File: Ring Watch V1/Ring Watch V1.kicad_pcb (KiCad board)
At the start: 2 copper layers, 28 x 20.8 mm, 12 parts, among them J1 Programming Header, J2 CR2023 Socket, U1 ATtiny85-20SU, U2 PCF8523T, Y1 32.768

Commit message: almost done placing components
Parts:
- C2: moved to F.Cu
- J1: footprint Connector_PinHeader_2.54mm:PinHeader_2x03_P2.54mm_Vertical -> Connector_PinHeader_1.00mm:PinHeader_2x03_P1.00mm_Vertical
- moved C1 20.2 mm to (108.7, 112.3), turned to 90 degrees
- moved R1 16.1 mm to (100.1, 107.4), turned to 270 degrees
- moved C2 13.8 mm to (97.4, 113.5)
- moved R3 13.0 mm to (108.5, 105.7), turned to 270 degrees
- moved J1 12.9 mm to (112.0, 109.0)
- moved U1 1.53 mm to (104.3, 109.1), turned to 270 degrees
- moved U2 0.51 mm to (95.9, 108.5)
- moved Y1 0.51 mm to (90.8, 108.5)
- moved R2 0.41 mm to (104.4, 102.6)
- moved D1 0.35 mm to (98.3, 101.5)
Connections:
- J1 pad 5: B3 -> B5
- U2 pad 8: +BATT -> Net-(C1-Pad1)
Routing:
- net B2: track 0.00 -> 11.1 mm, vias 0 -> 1
- net B0: track 0.00 -> 10.0 mm
- net B4: track 0.00 -> 7.23 mm
- net B1: track 0.00 -> 7.18 mm
- net B3: track 0.00 -> 3.07 mm

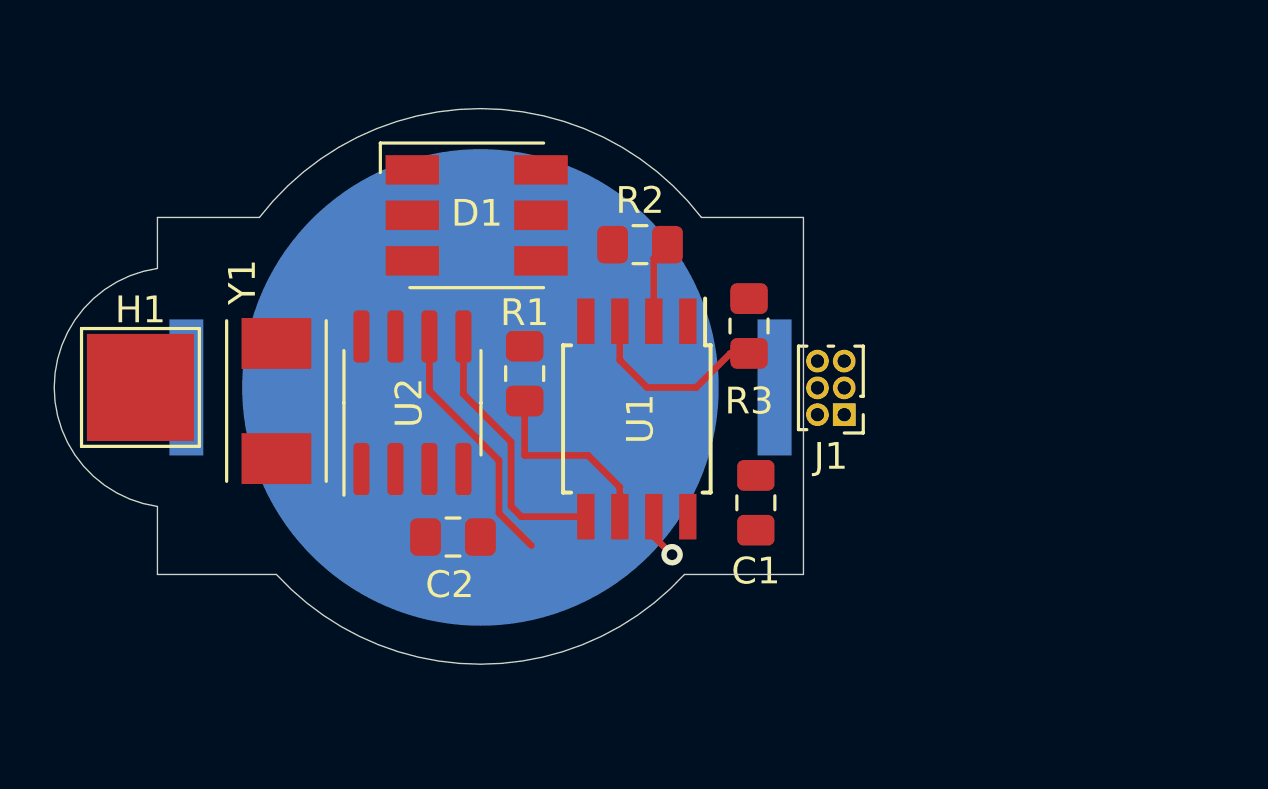
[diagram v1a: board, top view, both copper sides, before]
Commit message: modified component placement
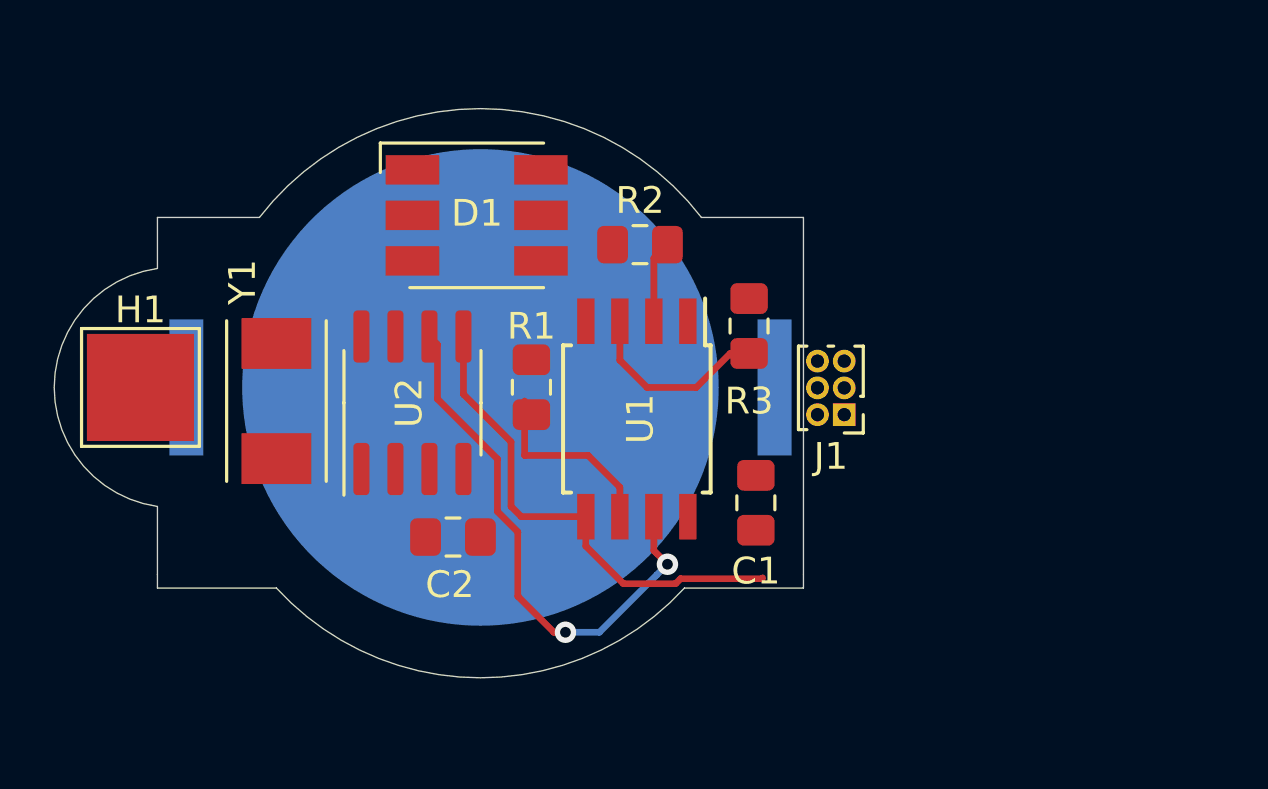
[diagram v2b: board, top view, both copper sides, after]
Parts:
- moved R1 0.57 mm to (100.3, 107.9)
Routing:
- net B2: track 11.1 -> 20.3 mm, vias 1 -> 2
- net B0: track 10.0 -> 18.4 mm
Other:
- board size 28 x 20.8 mm -> 28 x 21.3 mm
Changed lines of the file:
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@@
   (general
     (thickness 1.6)
-    (drawings 10)
-    (tracks 23)
+    (drawings 12)
+    (tracks 38)
     (zones 0)
     (modules 12)
@@
   )
   (module Resistor_SMD:R_0805_2012Metric_Pad1.15x1.40mm_HandSolder (layer F.Cu)
-    (at 100.076 107.433 270)
+    (at 100.33 107.941 270)
     (descr "Resistor SMD 0805 (2012 Metric), square (rectangular) end terminal, IPC_7351 nominal with elongated pad for handsoldering. (Body size source: https://docs.google.com/spreadsheets/d/1BsfQQcO9C6DZCsRaXUlFlo91Tg2WpOkGARC1WS5S8t0/edit?usp=sharing), generated with kicad-footprint-generator")
     (tags "resistor handsolder")
@@
     )
   )
+  (gr_line (start 86.36 114.935) (end 86.36 115.443) (layer Edge.Cuts) (width 0.05))
+  (gr_line (start 110.49 114.935) (end 110.49 115.443) (layer Edge.Cuts) (width 0.05))
+  (gr_arc (start 98.425 108.458) (end 90.805001 115.442999) (angle -94.97910584) (layer Edge.Cuts) (width 0.05))
+  (gr_line (start 110.49 115.443) (end 106.044999 115.442999) (layer Edge.Cuts) (width 0.05))
   (gr_line (start 86.359999 112.394999) (end 86.36 114.935) (layer Edge.Cuts) (width 0.05))
   (gr_line (start 86.36 101.6) (end 86.360001 103.505001) (layer Edge.Cuts) (width 0.05))
   (gr_arc (start 86.995 107.95) (end 86.360001 103.505001) (angle -163.7397953) (layer Edge.Cuts) (width 0.05))
-  (gr_line (start 90.805001 114.934999) (end 86.36 114.935) (layer Edge.Cuts) (width 0.05))
-  (gr_line (start 110.49 114.935) (end 106.044999 114.934999) (layer Edge.Cuts) (width 0.05))
+  (gr_line (start 90.805001 115.442999) (end 86.36 115.443) (layer Edge.Cuts) (width 0.05))
   (gr_line (start 106.679999 101.600001) (end 110.49 101.6) (layer Edge.Cuts) (width 0.05))
   (gr_line (start 86.36 101.6) (end 90.17 101.6) (layer Edge.Cuts) (width 0.05))
-  (gr_arc (start 98.425 107.95) (end 90.805001 114.934999) (angle -94.97910584) (layer Edge.Cuts) (width 0.05))
   (gr_arc (start 98.425 107.95) (end 106.679999 101.600001) (angle -104.8628159) (layer Edge.Cuts) (width 0.05))
   (gr_line (start 110.49 101.6) (end 110.49 114.935) (layer Edge.Cuts) (width 0.05))
@@
   (segment (start 99.95041 112.776) (end 102.362 112.776) (width 0.25) (layer F.Cu) (net 6))
   (segment (start 99.568 112.39359) (end 99.95041 112.776) (width 0.25) (layer F.Cu) (net 6))
+  (segment (start 105.900022 115.09299) (end 108.93501 115.09299) (width 0.25) (layer F.Cu) (net 6))
+  (segment (start 105.71399 115.279022) (end 105.900022 115.09299) (width 0.25) (layer F.Cu) (net 6))
+  (segment (start 103.765021 115.279021) (end 105.71399 115.279022) (width 0.25) (layer F.Cu) (net 6))
+  (segment (start 102.362 112.776) (end 102.362 113.876) (width 0.25) (layer F.Cu) (net 6))
+  (segment (start 102.362 113.876) (end 103.765021 115.279021) (width 0.25) (layer F.Cu) (net 6))
+  (segment (start 108.93501 115.09299) (end 108.966 115.062) (width 0.25) (layer F.Cu) (net 6))
   (segment (start 103.632 111.676) (end 103.632 112.776) (width 0.25) (layer F.Cu) (net 7))
-  (segment (start 102.446 110.49) (end 103.632 111.676) (width 0.25) (layer F.Cu) (net 7))
   (segment (start 100.076 110.49) (end 102.446 110.49) (width 0.25) (layer F.Cu) (net 7))
   (segment (start 100.076 108.458) (end 100.076 110.49) (width 0.25) (layer F.Cu) (net 7))
-  (via (at 105.582536 114.196577) (size 0.8) (drill 0.4) (layers F.Cu B.Cu) (net 8))
-  (segment (start 104.902 112.776) (end 104.902 113.516041) (width 0.25) (layer F.Cu) (net 8))
-  (segment (start 104.902 113.516041) (end 105.582536 114.196577) (width 0.25) (layer F.Cu) (net 8))
-  (segment (start 99.11799 110.679222) (end 99.11799 112.6428) (width 0.25) (layer F.Cu) (net 8))
-  (segment (start 99.11799 112.6428) (end 100.33 113.85481) (width 0.25) (layer F.Cu) (net 8))
-  (segment (start 96.52 108.081232) (end 99.11799 110.679222) (width 0.25) (layer F.Cu) (net 8))
-  (segment (start 96.52 106.048) (end 96.52 108.081232) (width 0.25) (layer F.Cu) (net 8))
+  (segment (start 102.446 110.49) (end 103.632 111.676) (width 0.25) (layer F.Cu) (net 7))
+  (segment (start 96.52 106.048) (end 96.82 106.348) (width 0.25) (layer F.Cu) (net 8))
+  (segment (start 99.06 112.58481) (end 99.822 113.34681) (width 0.25) (layer F.Cu) (net 8))
+  (segment (start 99.06 110.621232) (end 99.06 112.58481) (width 0.25) (layer F.Cu) (net 8))
+  (segment (start 96.82 108.381232) (end 99.06 110.621232) (width 0.25) (layer F.Cu) (net 8))
+  (segment (start 96.82 106.348) (end 96.82 108.381232) (width 0.25) (layer F.Cu) (net 8))
+  (via (at 101.6 117.094) (size 0.8) (drill 0.4) (layers F.Cu B.Cu) (net 8))
+  (segment (start 101.165488 117.094) (end 101.6 117.094) (width 0.25) (layer F.Cu) (net 8))
+  (segment (start 99.822 113.34681) (end 99.822 115.750512) (width 0.25) (layer F.Cu) (net 8))
+  (segment (start 99.822 115.750512) (end 101.165488 117.094) (width 0.25) (layer F.Cu) (net 8))
+  (segment (start 105.010001 114.154001) (end 105.41 114.554) (width 0.25) (layer F.Cu) (net 8))
+  (segment (start 101.6 117.094) (end 102.87 117.094) (width 0.25) (layer B.Cu) (net 8))
+  (segment (start 102.87 117.094) (end 105.010001 114.953999) (width 0.25) (layer B.Cu) (net 8))
+  (via (at 105.41 114.554) (size 0.8) (drill 0.4) (layers F.Cu B.Cu) (net 8))
+  (segment (start 105.010001 114.953999) (end 105.41 114.554) (width 0.25) (layer B.Cu) (net 8))
+  (segment (start 104.902 114.046) (end 105.010001 114.154001) (width 0.25) (layer F.Cu) (net 8))
+  (segment (start 104.902 112.776) (end 104.902 114.046) (width 0.25) (layer F.Cu) (net 8))
   (segment (start 104.902 103.124) (end 105.41 102.616) (width 0.25) (layer F.Cu) (net 9))
   (segment (start 104.902 105.476) (end 104.902 103.124) (width 0.25) (layer F.Cu) (net 9))

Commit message: more routing, board shape near final
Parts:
- moved R3 3.04 mm to (108.5, 102.6), turned to 0 degrees
- moved J1 2.81 mm to (109.2, 109.2)
- moved R1 1.03 mm to (100.1, 106.9)
- moved C1 0.57 mm to (108.5, 112.8)
- moved C2 0.46 mm to (97.0, 113.8)
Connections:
- J1 pad 1: +BATT -> Net-(C1-Pad1)
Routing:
- net +BATT: track 0.00 -> 51.0 mm, vias 0 -> 1
- net Net-(C1-Pad1): track 0.00 -> 44.8 mm, vias 0 -> 2
- net Net-(D1-Pad6): track 0.00 -> 8.32 mm
- net Net-(U2-Pad2): track 0.00 -> 7.56 mm
- net Net-(U2-Pad1): track 0.00 -> 6.75 mm
- net Net-(D1-Pad5): track 0.00 -> 3.54 mm
- net B4: track 7.23 -> 10.2 mm
- net Net-(D1-Pad4): track 0.00 -> 2.95 mm
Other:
- board size 28 x 21.3 mm -> 31.8 x 25.4 mm

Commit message: more layout changes uuggh
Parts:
- H1: footprint TestPoint:TestPoint_Pad_4.0x4.0mm -> TestPoint:TestPoint_Keystone_5019_Minature
- moved R3 4.44 mm to (104.4, 100.8)
- moved C1 3.82 mm to (108.2, 109.0)
- moved J1 3.30 mm to (108.0, 112.3), turned to 0 degrees
- moved H1 2.17 mm to (87.9, 108.2), turned to 270 degrees
- moved Y1 0.65 mm to (91.4, 108.6)
- moved R2 0.51 mm to (104.4, 103.1)
- moved U2 0.51 mm to (96.4, 108.5)
- moved R1 0.25 mm to (100.3, 106.9)
- moved D1 0.15 mm to (98.4, 101.5)
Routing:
- net B5: track 0.00 -> 12.4 mm, vias 0 -> 1
- net B1: track 6.69 -> 14.7 mm
- net B2: track 20.0 -> 27.2 mm
- net Net-(D1-Pad6): track 8.32 -> 3.10 mm
- net B0: track 18.4 -> 23.3 mm
- net B4: track 10.2 -> 13.1 mm
- net Net-(C1-Pad1): track 44.8 -> 44.3 mm
- net B3: track 3.07 -> 2.56 mm
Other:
- board size 31.8 x 25.4 mm -> 24.1 x 25.4 mm

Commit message: more layout changes
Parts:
- moved R1 5.51 mm to (103.4, 102.4)
- moved R3 3.41 mm to (107.4, 102.4), turned to 270 degrees
- moved R2 1.28 mm to (105.4, 102.4), turned to 270 degrees
- moved D1 0.86 mm to (98.4, 100.7)
- moved U1 0.76 mm to (103.5, 109.1)
- moved C1 0.25 mm to (108.5, 109.0)
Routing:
- net B1: track 14.7 -> 20.9 mm
- net Net-(D1-Pad6): track 3.10 -> 7.58 mm
- net B4: track 13.1 -> 10.8 mm
- net Net-(D1-Pad5): track 3.34 -> 5.67 mm
- net Net-(C1-Pad1): track 44.3 -> 45.3 mm
- net B5: track 12.4 -> 13.2 mm
- net B0: track 23.3 -> 22.6 mm
- net Net-(D1-Pad4): track 2.91 -> 3.48 mm

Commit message: minor changes, need to place GND polygons
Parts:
- added C3: 2.2uf, Capacitor_SMD:C_0805_2012Metric_Pad1.15x1.40mm_HandSolder, F.Cu at (92.7, 104.1)
- moved H1 0.76 mm to (87.9, 109.0)
- moved U2 0.51 mm to (96.4, 109.0)
- moved Y1 0.51 mm to (91.4, 109.1)
- moved C2 0.51 mm to (97.0, 114.3)
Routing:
- net +BATT: track 50.6 -> 51.1 mm
- net B2: track 27.5 -> 27.0 mm
- net B0: track 22.6 -> 22.1 mm

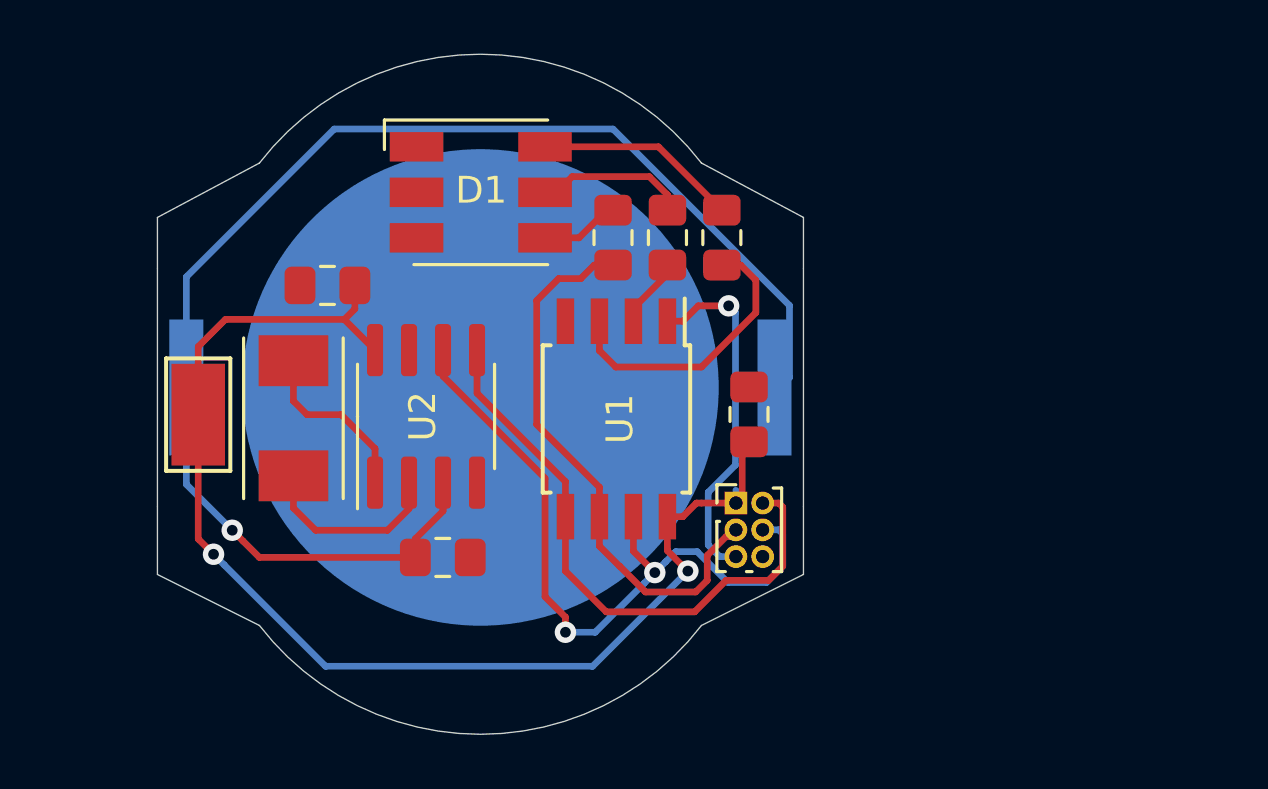
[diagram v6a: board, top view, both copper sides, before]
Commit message: added vdd cap, ground pours
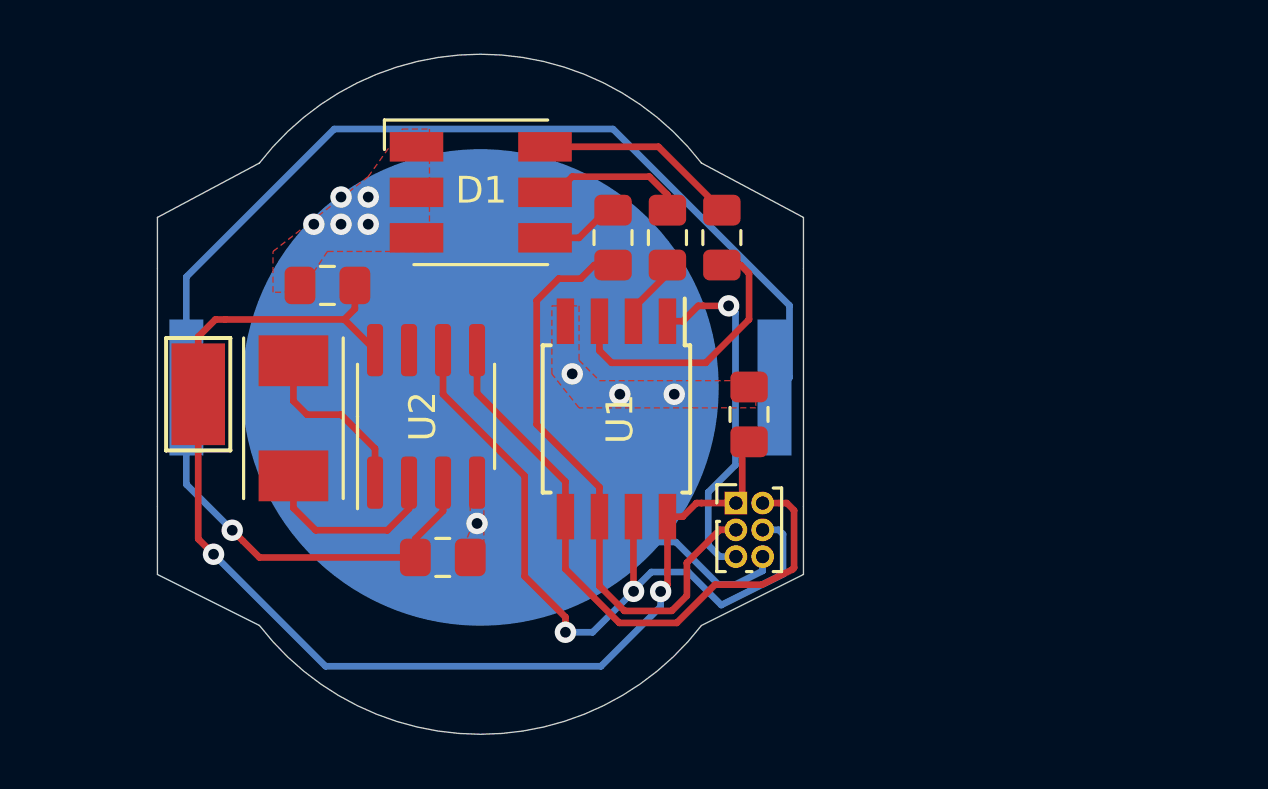
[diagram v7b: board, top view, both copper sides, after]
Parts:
- moved H1 0.76 mm to (87.9, 108.2)
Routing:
- net GND: track 0.00 -> 14.2 mm, vias 0 -> 9
- net B1: track 20.9 -> 22.5 mm
- net Net-(C1-Pad1): track 45.3 -> 44.0 mm
- net B0: track 22.1 -> 23.1 mm
- added copper zone on F.Cu, net GND

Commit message: added name and title in silkscreen
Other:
- board text added: "Ring Watch V1 salazarj"
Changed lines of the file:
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@@
   (general
     (thickness 1.6)
-    (drawings 12)
+    (drawings 13)
     (tracks 144)
     (zones 0)
@@
     )
   )
+  (gr_text "Ring Watch V1\nsalazarj" (at 96.52 117.348) (layer F.SilkS)
+    (effects (font (size 0.75 0.75) (thickness 0.1875)))
+  )
   (gr_line (start 110.49 103.505001) (end 110.489998 112.394999) (layer Edge.Cuts) (width 0.05))
   (gr_line (start 86.360001 103.505001) (end 86.359999 112.394999) (layer Edge.Cuts) (width 0.05))
@@
   (gr_line (start 86.36 101.6) (end 86.360001 103.505001) (layer Edge.Cuts) (width 0.05))
   (gr_arc (start 98.425 105.917999) (end 106.679999 99.568) (angle -104.8628159) (layer Edge.Cuts) (width 0.05))
-  (via (at 105.664 108.204) (size 0.8) (drill 0.4) (layers F.Cu B.Cu) (net 2))
-  (via (at 103.632 108.204) (size 0.8) (drill 0.4) (layers F.Cu B.Cu) (net 2))
-  (via (at 101.854 107.442) (size 0.8) (drill 0.4) (layers F.Cu B.Cu) (net 2))
-  (via (at 92.202 101.854) (size 0.8) (drill 0.4) (layers F.Cu B.Cu) (net 2))
-  (via (at 93.218 100.838) (size 0.8) (drill 0.4) (layers F.Cu B.Cu) (net 2))
-  (via (at 94.234 100.838) (size 0.8) (drill 0.4) (layers F.Cu B.Cu) (net 2))
-  (via (at 93.218 101.854) (size 0.8) (drill 0.4) (layers F.Cu B.Cu) (net 2))
-  (via (at 94.234 101.854) (size 0.8) (drill 0.4) (layers F.Cu B.Cu) (net 2))
-  (via (at 98.298 113.03) (size 0.8) (drill 0.4) (layers F.Cu B.Cu) (net 2))
   (segment (start 109.970001 107.580001) (end 109.830002 107.72) (width 0.25) (layer B.Cu) (net 1))
   (segment (start 87.44 103.822) (end 92.964 98.298) (width 0.25) (layer B.Cu) (net 1))
@@
   (segment (start 89.553999 113.684009) (end 89.154 113.28401) (width 0.25) (layer F.Cu) (net 1))
   (segment (start 90.16999 114.3) (end 89.553999 113.684009) (width 0.25) (layer F.Cu) (net 1))
+  (via (at 105.664 108.204) (size 0.8) (drill 0.4) (layers F.Cu B.Cu) (net 2))
+  (via (at 103.632 108.204) (size 0.8) (drill 0.4) (layers F.Cu B.Cu) (net 2))
+  (via (at 101.854 107.442) (size 0.8) (drill 0.4) (layers F.Cu B.Cu) (net 2))
+  (via (at 92.202 101.854) (size 0.8) (drill 0.4) (layers F.Cu B.Cu) (net 2))
+  (via (at 93.218 100.838) (size 0.8) (drill 0.4) (layers F.Cu B.Cu) (net 2))
+  (via (at 94.234 100.838) (size 0.8) (drill 0.4) (layers F.Cu B.Cu) (net 2))
+  (via (at 93.218 101.854) (size 0.8) (drill 0.4) (layers F.Cu B.Cu) (net 2))
+  (via (at 94.234 101.854) (size 0.8) (drill 0.4) (layers F.Cu B.Cu) (net 2))
+  (via (at 98.298 113.03) (size 0.8) (drill 0.4) (layers F.Cu B.Cu) (net 2))
   (segment (start 108.966 114.802552) (end 107.939101 115.316) (width 0.25) (layer B.Cu) (net 2))
   (segment (start 107.31641 115.316) (end 105.723401 113.722991) (width 0.25) (layer B.Cu) (net 2))
